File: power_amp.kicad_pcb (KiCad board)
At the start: 2 copper layers, 100 x 70 mm, 59 parts, among them J1 Barrel_Jack_Switch, J2 Barrel_Jack_Switch, J3 Conn_Coaxial, J4 Conn_Coaxial, J5 AudioJack3_SwitchTR, J6 Conn_Coaxial, J7 Conn_Coaxial, Q1 Q_NPN_ECB, Q2 Q_PNP_ECB, Q3 Q_NPN_ECB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

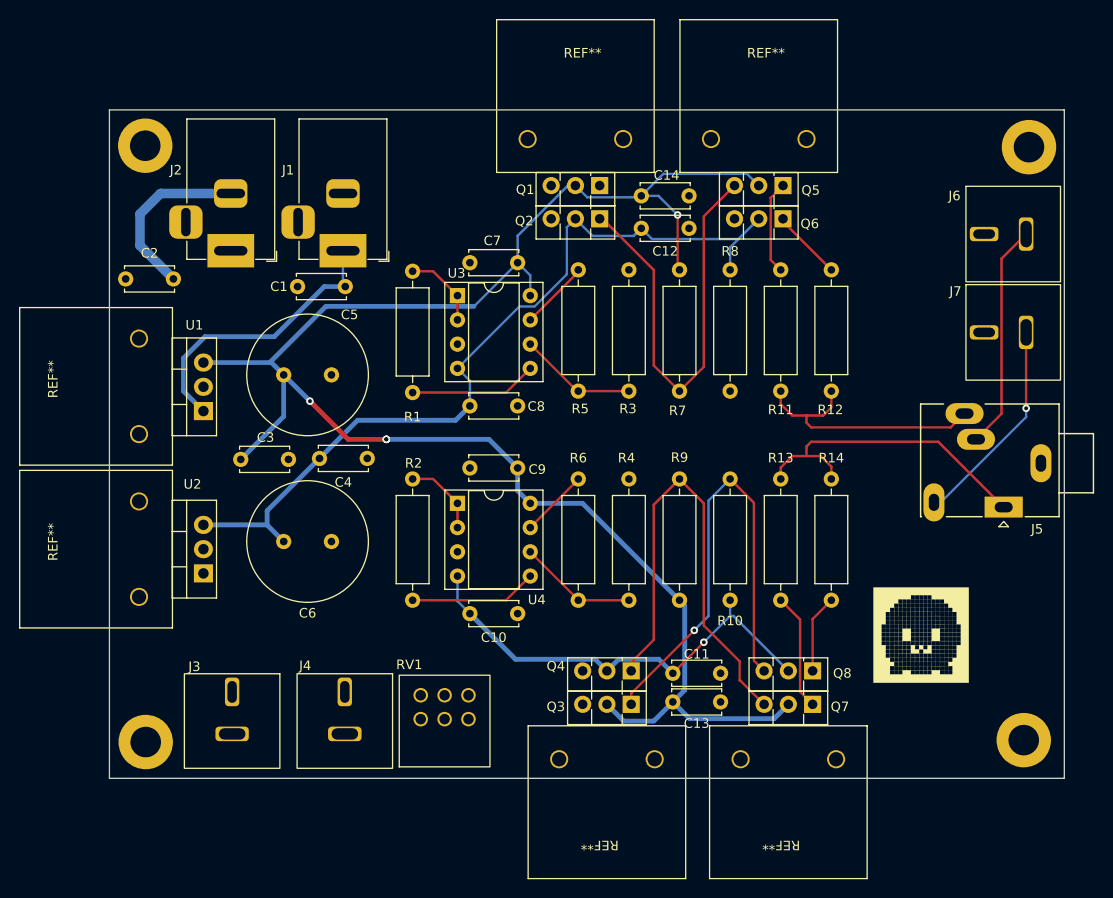
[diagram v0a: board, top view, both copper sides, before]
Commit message: made power-line 1mm
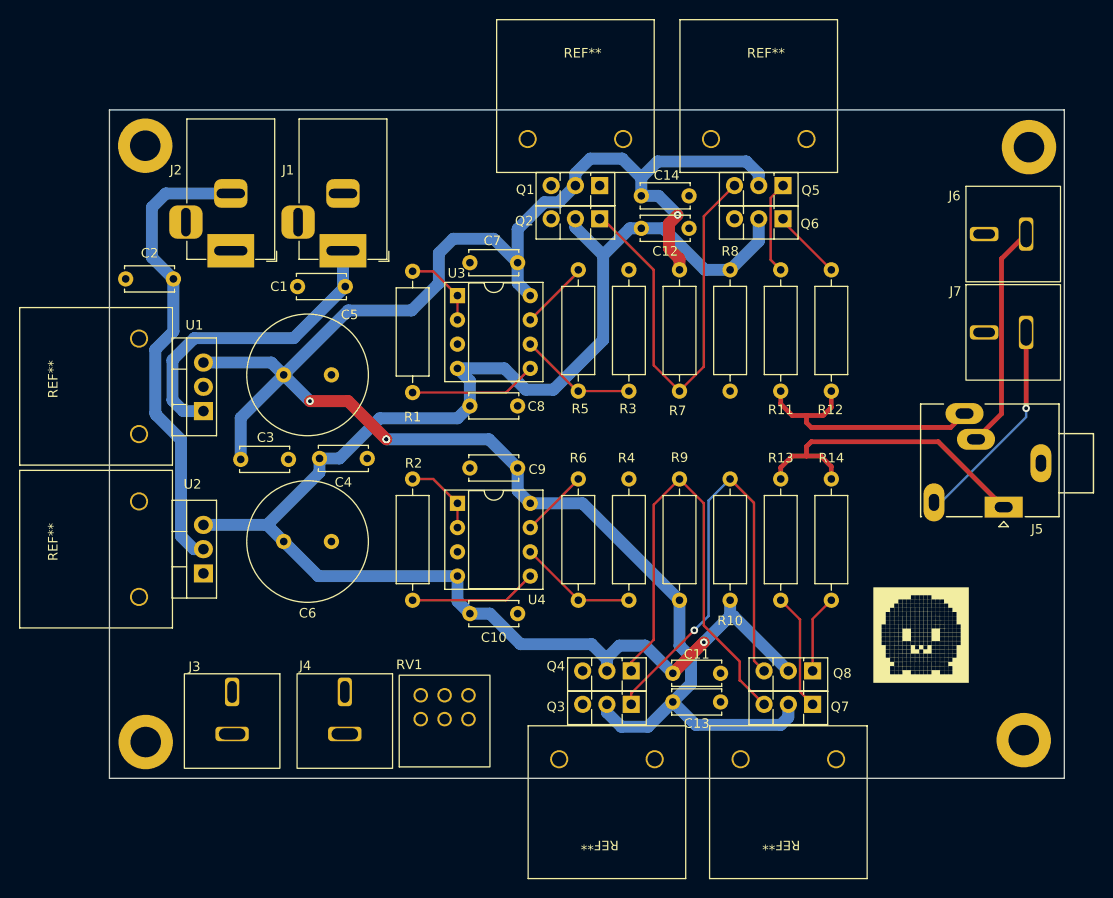
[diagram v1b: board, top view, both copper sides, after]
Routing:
- net -6V: track 18.6 -> 49.0 mm
- net -5V: track 135.7 -> 165.1 mm
- net +5V: track 182.4 -> 196.2 mm
- net +6V: track 30.3 -> 33.1 mm
